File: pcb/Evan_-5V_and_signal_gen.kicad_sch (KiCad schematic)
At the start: 28 parts, among them IC1 TL7660IDGKR, IC2 TL081IDT, IC4 UA78M33CDCYG3, J2 M22-6003005, U5 TPS2069CDBVR_MOSFET

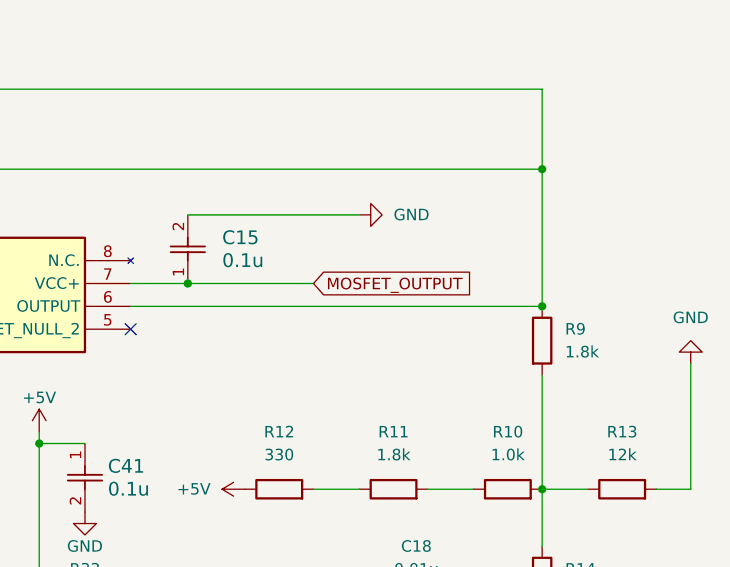
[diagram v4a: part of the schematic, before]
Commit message: MOSFET connections updated (#13)
* MOSFET connections updated

updated the MOSFET connection to control the 5V plane and added a separate line going directly to the 3.3V regulator.

* rotate U5 silk

---------

Co-authored-by: Karim Ait-Allaoua <kaitallaoua@gmail.com>
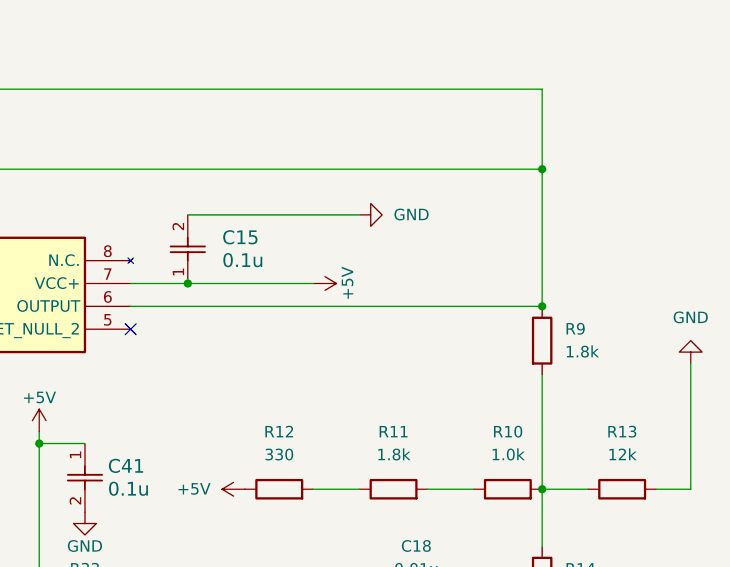
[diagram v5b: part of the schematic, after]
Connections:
- net +5V: now also C15.1, IC2.7 (VCC+)
- net MOSFET_OUTPUT: no longer C15.1, IC2.7 (VCC+)
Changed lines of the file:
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@@
-    )
-  )
-  (global_label "MOSFET_OUTPUT" (shape input) (at 237.49 68.58 0) (fields_autoplaced)
-    (effects (font (size 1.27 1.27)) (justify left))
-    (property "Intersheetrefs" "${INTERSHEET_REFS}" (at 255.8361 68.58 0)
-      (effects (font (size 1.27 1.27)) (justify left) hide)
     )
   )
@@
         )
       )
+    )
+  )
+  (symbol (lib_id "power:+5V") (at 237.49 68.58 270) (unit 1)
+    (in_bom yes) (on_board yes) (dnp no)
+    (property "Reference" "#PWR012" (at 233.68 68.58 0)
+      (effects (font (size 1.27 1.27)) hide)
+    )
+    (property "Value" "+5V" (at 241.3 68.58 0)
+      (effects (font (size 1.27 1.27)))
+    )
+    (property "Footprint" "" (at 237.49 68.58 0)
+      (effects (font (size 1.27 1.27)) hide)
+    )
+    (property "Datasheet" "" (at 237.49 68.58 0)
+      (effects (font (size 1.27 1.27)) hide)
+    )
+    (pin "1")
+    (instances
+      (project "mcu_integration"
+        (path "/c0210bc3-f67f-47d8-a34e-f002a728adb2/39708197-8fe0-4b5c-ba49-65ed06982da9"
+          (reference "#PWR012") (unit 1)
+        )
+      )

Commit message: update README with images, add BOM, schematic pdf, update evan sch title (#15)
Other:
- title: (none) -> Power and Sine Generator
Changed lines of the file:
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@@
 (kicad_sch (version 20230121) (generator eeschema)
   (paper "A4")
+  (title_block
+    (title "Power and Sine Generator")
+  )
   (junction (at 262.89 71.12) (diameter 0) (color 0 0 0 0)
   )

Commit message: done layout/ratsnet
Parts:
- C12, C13: footprint (none) -> capstone:T495D
- C17, C18, C25: footprint (none) -> capstone:C0805
- IC4: footprint (none) -> capstone:SOT230P700X180-4N
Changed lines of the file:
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@@
       (effects (font (size 1.27 1.27)) (justify right))
     )
-    (property "Footprint" "" (at 178.74 44.45 0)
+    (property "Footprint" "capstone:T495D" (at 178.74 44.45 0)
       (effects (font (size 1.27 1.27)) (justify left top) hide)
     )
@@
       (effects (font (size 1.27 1.27)) (justify right))
     )
-    (property "Footprint" "" (at 243.51 31.75 0)
+    (property "Footprint" "capstone:C0805" (at 243.51 31.75 0)
       (effects (font (size 1.27 1.27)) (justify left top) hide)
     )
@@
       (effects (font (size 1.27 1.27)) (justify left))
     )
-    (property "Footprint" "" (at -80.95 38.1 0)
+    (property "Footprint" "capstone:T495D" (at -80.95 38.1 0)
       (effects (font (size 1.27 1.27)) (justify left top) hide)
     )
@@
       (effects (font (size 1.27 1.27)))
     )
-    (property "Footprint" "" (at 251.46 201.6 0)
+    (property "Footprint" "capstone:C0805" (at 251.46 201.6 0)
       (effects (font (size 1.27 1.27)) (justify left top) hide)
     )
@@
       (effects (font (size 1.27 1.27)) (justify left))
     )
-    (property "Footprint" "" (at -46.66 96.52 0)
+    (property "Footprint" "capstone:C0805" (at -46.66 96.52 0)
       (effects (font (size 1.27 1.27)) (justify left top) hide)
     )
@@
       (effects (font (size 1.27 1.27)))
     )
-    (property "Footprint" "" (at 111.76 185.09 0)
-      (effects (font (size 1.27 1.27)) (justify left top) hide)
-    )
+    (property "Footprint" "capstone:SOT230P700X180-4N" (at 111.76 185.09 0)
+      (effects (font (size 1.27 1.27)) (justify left top) hide)
+    )

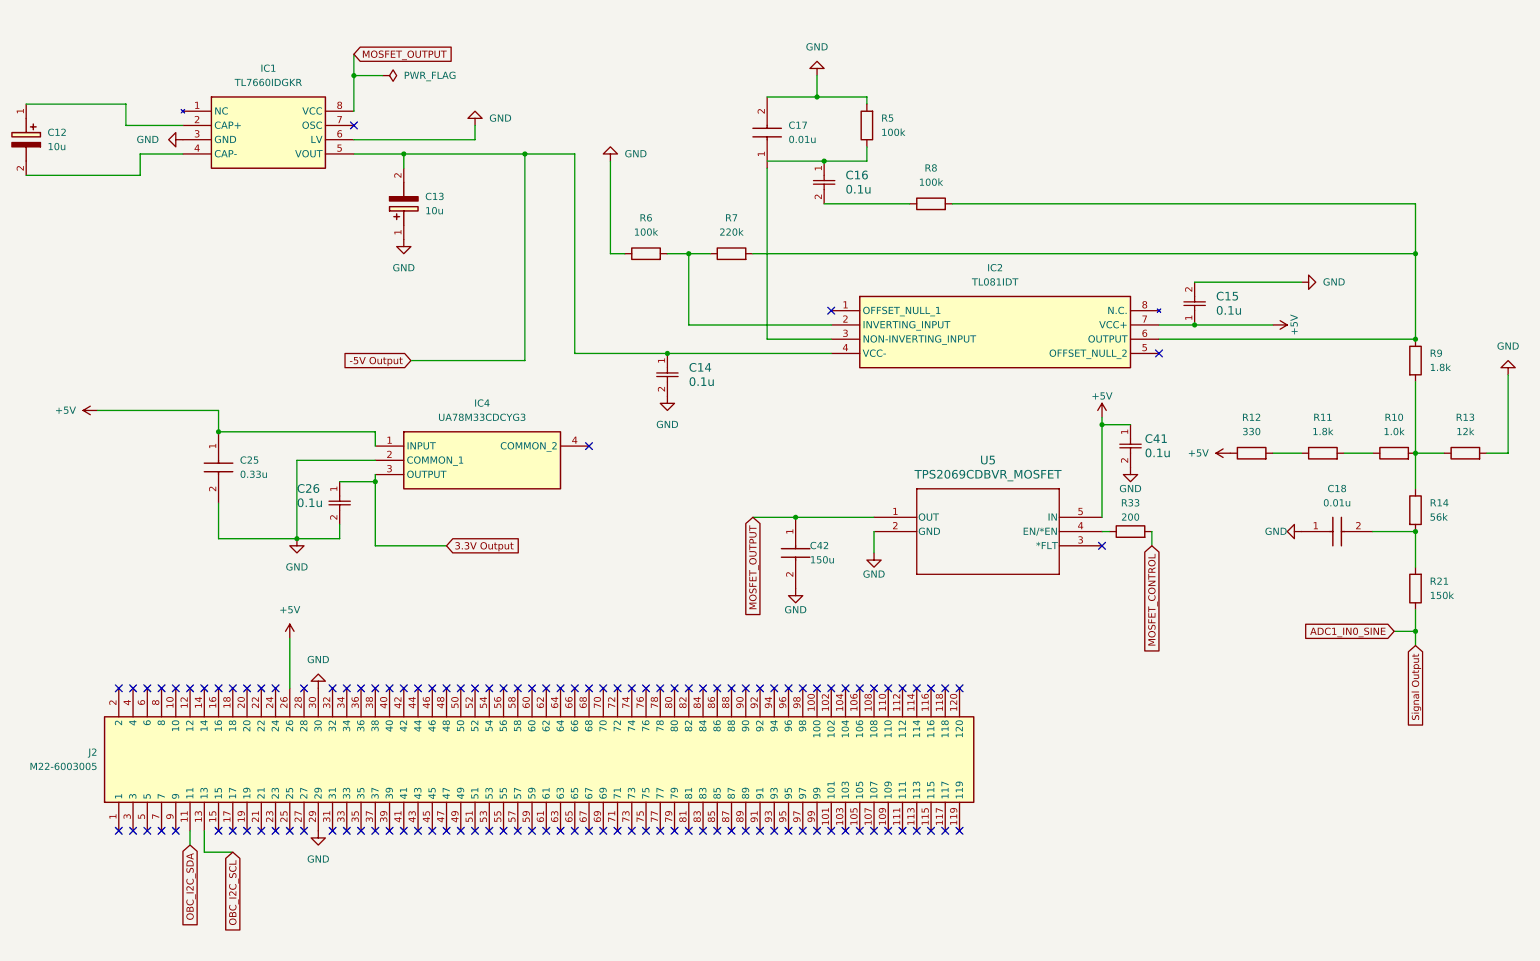
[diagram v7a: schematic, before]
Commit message: fix +5v connection, make final via
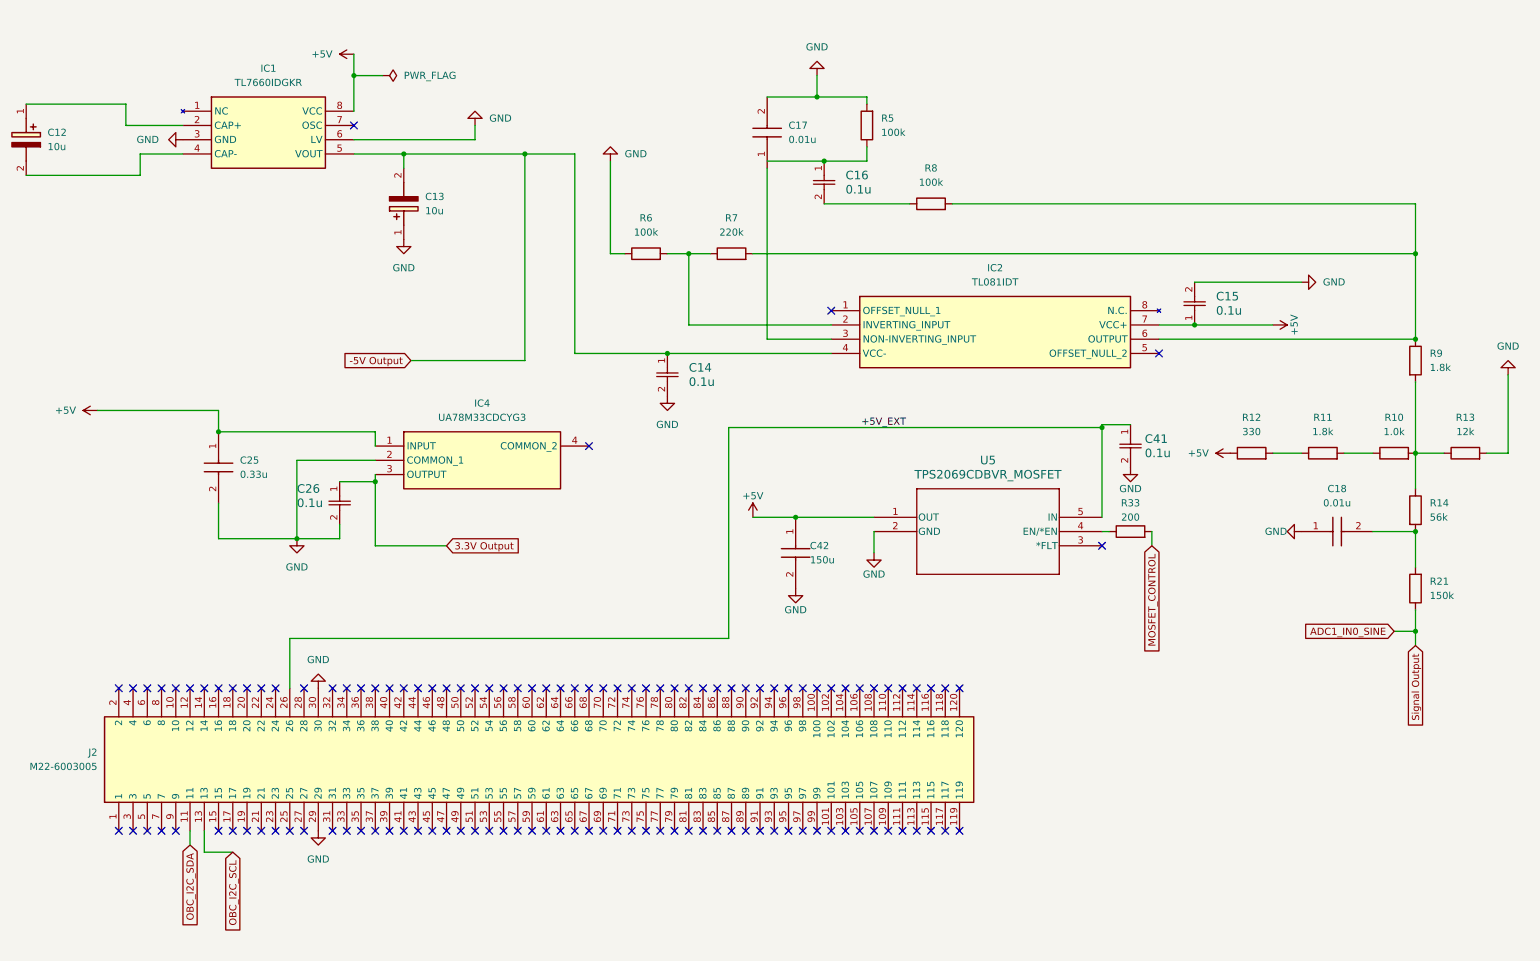
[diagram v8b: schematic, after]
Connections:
- net MOSFET_OUTPUT is gone; now on net +5V: C42.1, IC1.8 (VCC), U5.1 (OUT)
- net +5V: no longer C41.1, J2.26, U5.5 (IN)
- new net +5V_EXT: C41.1, J2.26, U5.5 (IN)
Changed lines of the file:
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@@
   (junction (at 133.35 55.88) (diameter 0) (color 0 0 0 0)
   )
+  (junction (at 207.01 86.868) (diameter 0) (color 0 0 0 0)
+  )
   (junction (at 262.89 105.41) (diameter 0) (color 0 0 0 0)
   )
@@
   )
   (junction (at 156.21 27.94) (diameter 0) (color 0 0 0 0)
-  )
-  (junction (at 207.01 86.36) (diameter 0) (color 0 0 0 0)
   )
   (junction (at 104.14 38.1) (diameter 0) (color 0 0 0 0)
@@
     (stroke (width 0) (type default))
   )
+  (wire (pts (xy 62.23 124.46) (xy 140.462 124.46))
+    (stroke (width 0) (type default))
+  )
   (wire (pts (xy 77.47 96.52) (xy 77.47 95.25))
     (stroke (width 0) (type default))
@@
     (stroke (width 0) (type default))
   )
+  (wire (pts (xy 140.462 86.868) (xy 207.01 86.868))
+    (stroke (width 0) (type default))
+  )
   (wire (pts (xy 104.14 38.1) (xy 104.14 74.93))
     (stroke (width 0) (type default))
@@
     (stroke (width 0) (type default))
   )
-  (wire (pts (xy 207.01 86.36) (xy 207.01 102.87))
+  (wire (pts (xy 207.01 86.36) (xy 207.01 86.868))
     (stroke (width 0) (type default))
   )
@@
     (stroke (width 0) (type default))
   )
+  (wire (pts (xy 207.01 86.868) (xy 207.01 102.87))
+    (stroke (width 0) (type default))
+  )
   (wire (pts (xy 82.55 38.1) (xy 82.55 40.64))
     (stroke (width 0) (type default))
@@
     (stroke (width 0) (type default))
   )
+  (wire (pts (xy 140.462 124.46) (xy 140.462 86.868))
+    (stroke (width 0) (type default))
+  )
   (wire (pts (xy 262.89 78.74) (xy 262.89 91.44))
     (stroke (width 0) (type default))
@@
     (stroke (width 0) (type default))
   )
-  (wire (pts (xy 207.01 85.09) (xy 207.01 86.36))
-    (stroke (width 0) (type default))
-  )
   (wire (pts (xy 157.48 39.37) (xy 165.1 39.37))
     (stroke (width 0) (type default))
@@
   (wire (pts (xy 262.89 119.38) (xy 262.89 123.19))
     (stroke (width 0) (type default))
+  )
+  (label "+5V_EXT" (at 164.084 86.868 0) (fields_autoplaced)
+    (effects (font (size 1.27 1.27)) (justify left bottom))
   )
   (global_label "ADC1_IN0_SINE" (shape input) (at 259.08 123.19 180) (fields_autoplaced)
@@
     )
   )
-  (global_label "MOSFET_OUTPUT" (shape input) (at 144.78 102.87 270) (fields_autoplaced)
-    (effects (font (size 1.27 1.27)) (justify right))
-    (property "Intersheetrefs" "${INTERSHEET_REFS}" (at 144.78 121.2161 90)
-      (effects (font (size 1.27 1.27)) (justify right) hide)
-    )
-  )
   (global_label "OBC_I2C_SDA" (shape input) (at 44.45 161.29 270) (fields_autoplaced)
     (effects (font (size 1.27 1.27)) (justify right))
@@
     (property "Intersheetrefs" "${INTERSHEET_REFS}" (at 52.07 177.9428 90)
       (effects (font (size 1.27 1.27)) (justify right) hide)
-    )
-  )
-  (global_label "MOSFET_OUTPUT" (shape input) (at 73.66 20.32 0) (fields_autoplaced)
-    (effects (font (size 1.27 1.27)) (justify left))
-    (property "Intersheetrefs" "${INTERSHEET_REFS}" (at 92.0061 20.32 0)
-      (effects (font (size 1.27 1.27)) (justify left) hide)
     )
   )
@@
     )
   )
+  (symbol (lib_id "power:+5V") (at 144.78 102.87 0) (unit 1)
+    (in_bom yes) (on_board yes) (dnp no)
+    (property "Reference" "#PWR09" (at 144.78 106.68 0)
+      (effects (font (size 1.27 1.27)) hide)
+    )
+    (property "Value" "+5V" (at 144.78 99.06 0)
+      (effects (font (size 1.27 1.27)))
+    )
+    (property "Footprint" "" (at 144.78 102.87 0)
+      (effects (font (size 1.27 1.27)) hide)
+    )
+    (property "Datasheet" "" (at 144.78 102.87 0)
+      (effects (font (size 1.27 1.27)) hide)
+    )
+    (pin "1")
+    (instances
+      (project "mcu_integration"
+        (path "/c0210bc3-f67f-47d8-a34e-f002a728adb2/39708197-8fe0-4b5c-ba49-65ed06982da9"
+          (reference "#PWR09") (unit 1)
+        )
+      )
+    )
+  )
   (symbol (lib_id "Device:R") (at 246.38 91.44 90) (unit 1)
     (in_bom yes) (on_board yes) (dnp no) (fields_autoplaced)
@@
     )
   )
-  (symbol (lib_id "power:+5V") (at 207.01 85.09 0) (unit 1)
-    (in_bom yes) (on_board yes) (dnp no)
-    (property "Reference" "#PWR09" (at 207.01 88.9 0)
-      (effects (font (size 1.27 1.27)) hide)
-    )
-    (property "Value" "+5V" (at 207.01 81.28 0)
-      (effects (font (size 1.27 1.27)))
-    )
-    (property "Footprint" "" (at 207.01 85.09 0)
-      (effects (font (size 1.27 1.27)) hide)
-    )
-    (property "Datasheet" "" (at 207.01 85.09 0)
-      (effects (font (size 1.27 1.27)) hide)
-    )
-    (pin "1")
-    (instances
-      (project "mcu_integration"
-        (path "/c0210bc3-f67f-47d8-a34e-f002a728adb2/39708197-8fe0-4b5c-ba49-65ed06982da9"
-          (reference "#PWR09") (unit 1)
+  (symbol (lib_id "power:+5V") (at 73.66 20.32 90) (unit 1)
+    (in_bom yes) (on_board yes) (dnp no) (fields_autoplaced)
+    (property "Reference" "#PWR016" (at 77.47 20.32 0)
+      (effects (font (size 1.27 1.27)) hide)
+    )
+    (property "Value" "+5V" (at 69.85 20.32 90)
+      (effects (font (size 1.27 1.27)) (justify left))
+    )
+    (property "Footprint" "" (at 73.66 20.32 0)
+      (effects (font (size 1.27 1.27)) hide)
+    )
+    (property "Datasheet" "" (at 73.66 20.32 0)
+      (effects (font (size 1.27 1.27)) hide)
+    )
+    (pin "1")
+    (instances
+      (project "mcu_integration"
+        (path "/c0210bc3-f67f-47d8-a34e-f002a728adb2/39708197-8fe0-4b5c-ba49-65ed06982da9"
+          (reference "#PWR016") (unit 1)
         )
       )
@@
         )
       )
-    )
-  )
-  (symbol (lib_id "power:+5V") (at 62.23 124.46 0) (unit 1)
-    (in_bom yes) (on_board yes) (dnp no) (fields_autoplaced)
-    (property "Reference" "#PWR016" (at 62.23 128.27 0)
-      (effects (font (size 1.27 1.27)) hide)
-    )
-    (property "Value" "+5V" (at 62.23 119.38 0)
-      (effects (font (size 1.27 1.27)))
-    )
-    (property "Footprint" "" (at 62.23 124.46 0)
-      (effects (font (size 1.27 1.27)) hide)
-    )
-    (property "Datasheet" "" (at 62.23 124.46 0)
-      (effects (font (size 1.27 1.27)) hide)
-    )
-    (pin "1")
-    (instances
-      (project "mcu_integration"
-        (path "/c0210bc3-f67f-47d8-a34e-f002a728adb2/39708197-8fe0-4b5c-ba49-65ed06982da9"
-          (reference "#PWR016") (unit 1)
-        )
-      )
